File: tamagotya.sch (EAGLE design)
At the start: 62 parts, among them U100 ESP32-D2WD, U1000 TP4056, U1500 FS312F-G, U1550 FS8205, U200 UT-0206-P05FOLDED, U2000 MT3608, U2100 M3406, U300 4MB Flash, Y100 40Mhz 3.2X2.5

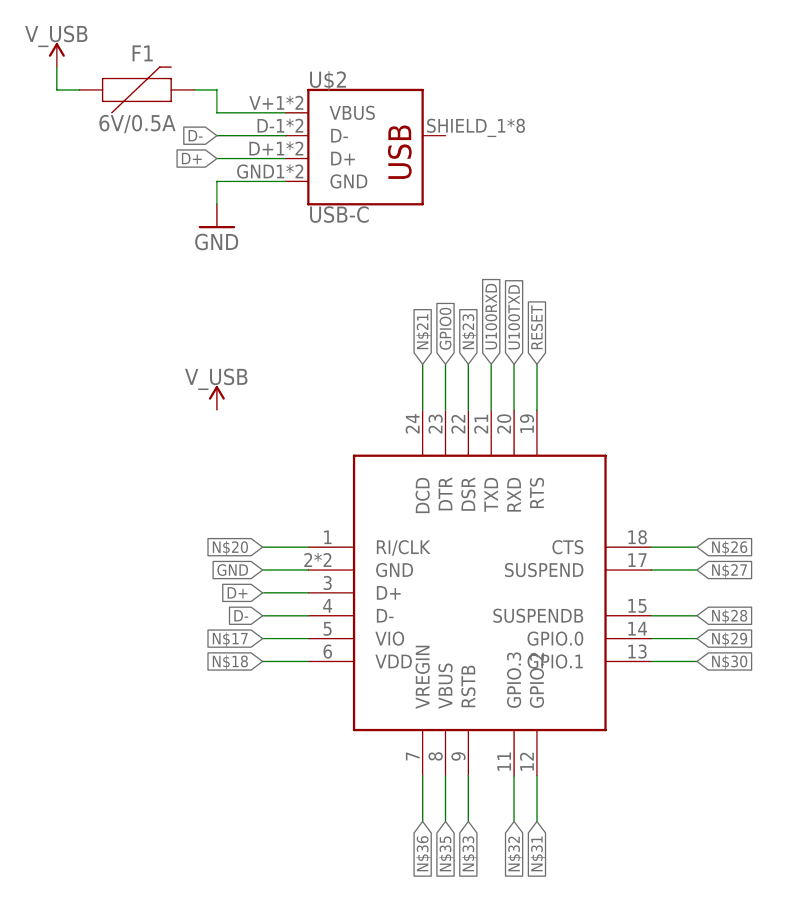
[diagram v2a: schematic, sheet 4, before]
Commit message: CP2102 now has adequate power circuitry, I believe
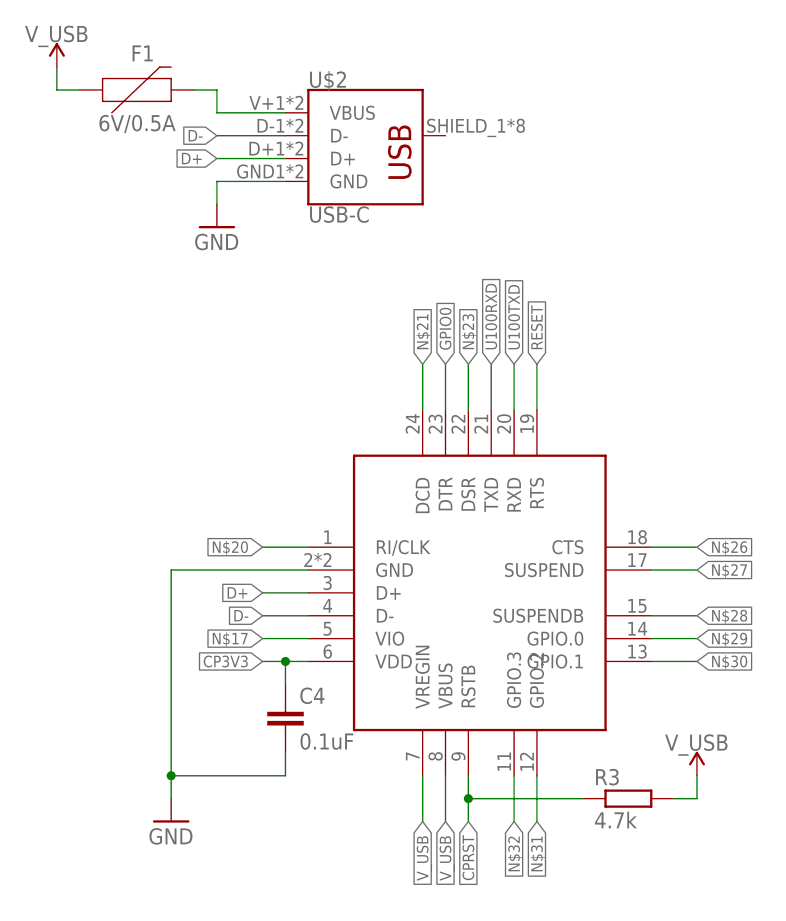
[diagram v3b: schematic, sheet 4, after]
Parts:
- added C4: 0.1uF, rcl:C-EUC0603
- added R3: 4.7k, rcl:R-EU_R0603
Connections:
- removed net N$18: U$3.VDD
- removed net N$33: U$3.RSTB
- removed net N$35: U$3.VBUS
- removed net N$36: U$3.VREGIN
- new net CP3V3: C4.1, U$3.VDD
- new net CPRST: R3.1, U$3.RSTB
- net GND: now also C4.2
- net V_USB: now also R3.2, U$3.VBUS, U$3.VREGIN
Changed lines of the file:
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@@
 <part name="GND27" library="SparkFun-PowerSymbols" library_urn="urn:adsk.eagle:library:530" deviceset="GND" device=""/>
 <part name="SUPPLY18" library="SparkFun-PowerSymbols" library_urn="urn:adsk.eagle:library:530" deviceset="3.3V" device=""/>
+<part name="C4" library="rcl" library_urn="urn:adsk.eagle:library:334" deviceset="C-EU" device="C0603" package3d_urn="urn:adsk.eagle:package:23616/2" value="0.1uF"/>
+<part name="GND28" library="supply1" library_urn="urn:adsk.eagle:library:371" deviceset="GND" device=""/>
+<part name="R3" library="rcl" library_urn="urn:adsk.eagle:library:334" deviceset="R-EU_" device="R0603" package3d_urn="urn:adsk.eagle:package:23555/2" value="4.7k"/>
 </parts>
 <sheets>
@@
 <attribute name="VALUE" x="15.24" y="119.634" size="1.778" layer="96" align="bottom-center"/>
 </instance>
-<instance part="SUPPLY17" gate="G$1" x="33.02" y="78.74" smashed="yes">
-<attribute name="VALUE" x="33.02" y="81.534" size="1.778" layer="96" align="bottom-center"/>
+<instance part="SUPPLY17" gate="G$1" x="86.36" y="38.1" smashed="yes">
+<attribute name="VALUE" x="86.36" y="40.894" size="1.778" layer="96" align="bottom-center"/>
+</instance>
+<instance part="C4" gate="G$1" x="40.64" y="45.72" smashed="yes">
+<attribute name="NAME" x="42.164" y="46.101" size="1.778" layer="95"/>
+<attribute name="VALUE" x="42.164" y="41.021" size="1.778" layer="96"/>
+</instance>
+<instance part="GND28" gate="1" x="27.94" y="33.02" smashed="yes">
+<attribute name="VALUE" x="25.4" y="30.48" size="1.778" layer="96"/>
+</instance>
+<instance part="R3" gate="G$1" x="78.74" y="35.56" smashed="yes">
+<attribute name="NAME" x="74.93" y="37.0586" size="1.778" layer="95"/>
+<attribute name="VALUE" x="74.93" y="32.258" size="1.778" layer="96"/>
 </instance>
 </instances>
@@
 </segment>
 <segment>
+<pinref part="C4" gate="G$1" pin="2"/>
+<wire x1="40.64" y1="40.64" x2="40.64" y2="38.1" width="0.1524" layer="91"/>
+<wire x1="40.64" y1="38.1" x2="27.94" y2="38.1" width="0.1524" layer="91"/>
+<pinref part="GND28" gate="1" pin="GND"/>
+<wire x1="27.94" y1="38.1" x2="27.94" y2="35.56" width="0.1524" layer="91"/>
 <pinref part="U$3" gate="G$1" pin="GND"/>
-<wire x1="43.18" y1="60.96" x2="38.1" y2="60.96" width="0.1524" layer="91"/>
-<label x="38.1" y="60.96" size="1.27" layer="95" rot="R180" xref="yes"/>
+<wire x1="43.18" y1="60.96" x2="27.94" y2="60.96" width="0.1524" layer="91"/>
+<wire x1="27.94" y1="60.96" x2="27.94" y2="38.1" width="0.1524" layer="91"/>
+<junction x="27.94" y="38.1"/>
 </segment>
 </net>
@@
 </segment>
 </net>
-<net name="N$18" class="0">
+<net name="CP3V3" class="0">
 <segment>
 <pinref part="U$3" gate="G$1" pin="VDD"/>
-<wire x1="43.18" y1="50.8" x2="38.1" y2="50.8" width="0.1524" layer="91"/>
+<wire x1="43.18" y1="50.8" x2="40.64" y2="50.8" width="0.1524" layer="91"/>
 <label x="38.1" y="50.8" size="1.27" layer="95" rot="R180" xref="yes"/>
+<pinref part="C4" gate="G$1" pin="1"/>
+<wire x1="40.64" y1="50.8" x2="38.1" y2="50.8" width="0.1524" layer="91"/>
+<wire x1="40.64" y1="48.26" x2="40.64" y2="50.8" width="0.1524" layer="91"/>
+<junction x="40.64" y="50.8"/>
 </segment>
 </net>
@@
 </segment>
 </net>
-<net name="N$33" class="0">
+<net name="CPRST" class="0">
 <segment>
 <pinref part="U$3" gate="G$1" pin="RSTB"/>
-<wire x1="60.96" y1="38.1" x2="60.96" y2="33.02" width="0.1524" layer="91"/>
+<wire x1="60.96" y1="38.1" x2="60.96" y2="35.56" width="0.1524" layer="91"/>
 <label x="60.96" y="33.02" size="1.27" layer="95" rot="R270" xref="yes"/>
-</segment>
-</net>
-<net name="N$35" class="0">
-<segment>
-<pinref part="U$3" gate="G$1" pin="VBUS"/>
-<wire x1="58.42" y1="38.1" x2="58.42" y2="33.02" width="0.1524" layer="91"/>
-<label x="58.42" y="33.02" size="1.27" layer="95" rot="R270" xref="yes"/>
-</segment>
-</net>
-<net name="N$36" class="0">
-<segment>
-<pinref part="U$3" gate="G$1" pin="VREGIN"/>
-<wire x1="55.88" y1="38.1" x2="55.88" y2="33.02" width="0.1524" layer="91"/>
-<label x="55.88" y="33.02" size="1.27" layer="95" rot="R270" xref="yes"/>
+<pinref part="R3" gate="G$1" pin="1"/>
+<wire x1="60.96" y1="35.56" x2="60.96" y2="33.02" width="0.1524" layer="91"/>
+<wire x1="73.66" y1="35.56" x2="60.96" y2="35.56" width="0.1524" layer="91"/>
+<junction x="60.96" y="35.56"/>
 </segment>
 </net>
@@
 <pinref part="SUPPLY13" gate="G$1" pin="V_USB"/>
 </segment>
-</net>
+<segment>
+<pinref part="U$3" gate="G$1" pin="VBUS"/>
+<wire x1="58.42" y1="38.1" x2="58.42" y2="33.02" width="0.1524" layer="91"/>
+<label x="58.42" y="33.02" size="1.27" layer="95" rot="R270" xref="yes"/>
+</segment>
+<segment>
+<pinref part="U$3" gate="G$1" pin="VREGIN"/>
+<wire x1="55.88" y1="38.1" x2="55.88" y2="33.02" width="0.1524" layer="91"/>
+<label x="55.88" y="33.02" size="1.27" layer="95" rot="R270" xref="yes"/>
+</segment>
+<segment>
+<pinref part="R3" gate="G$1" pin="2"/>
+<wire x1="83.82" y1="35.56" x2="86.36" y2="35.56" width="0.1524" layer="91"/>
+<pinref part="SUPPLY17" gate="G$1" pin="V_USB"/>
+<wire x1="86.36" y1="35.56" x2="86.36" y2="38.1" width="0.1524" layer="91"/>
+</segment>
+</net>

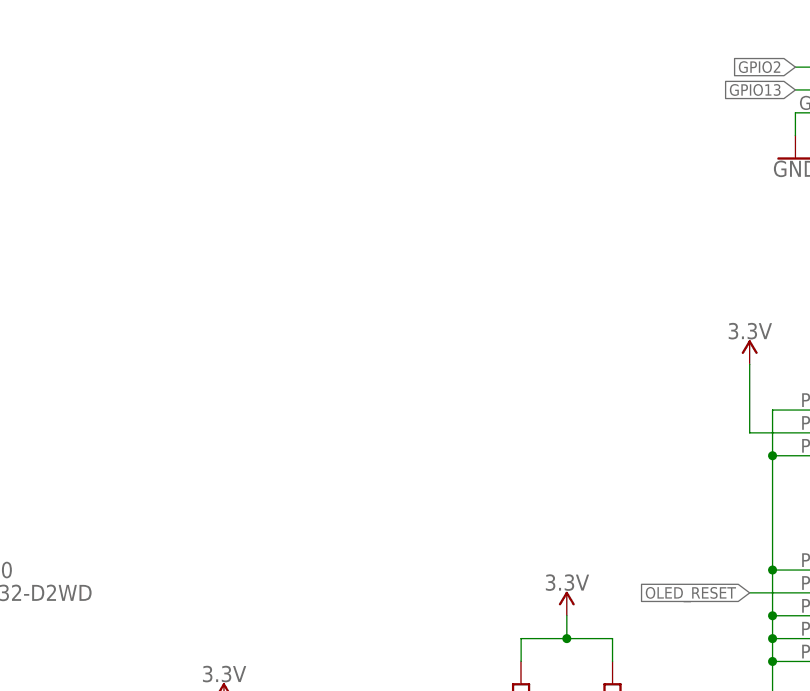
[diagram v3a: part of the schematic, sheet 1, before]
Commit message: Accellerometer ADXL345 with i2c + 1 interrupt.
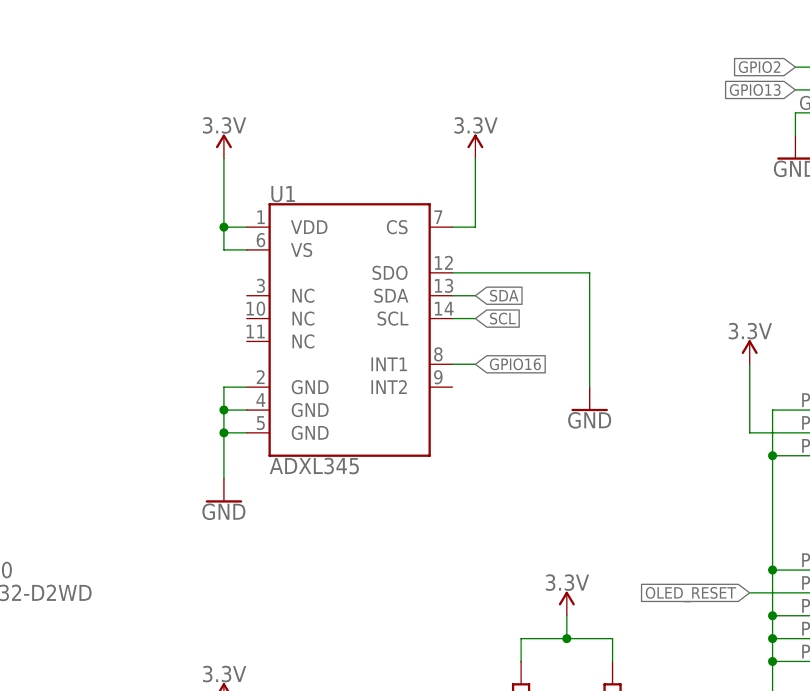
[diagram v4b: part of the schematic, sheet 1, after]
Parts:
- added U1: ADXL345, SparkFun-Sensors:ADXL345
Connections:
- net 3.3V: now also U1.CS, U1.VDD, U1.VS
- net GND: now also U1.GND@2, U1.GND@4, U1.GND@5, U1.SDO
- net GPIO16: now also U1.INT1
- net SCL: now also U1.SCL
- net SDA: now also U1.SDA
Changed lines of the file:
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@@
 <part name="GND28" library="supply1" library_urn="urn:adsk.eagle:library:371" deviceset="GND" device=""/>
 <part name="R3" library="rcl" library_urn="urn:adsk.eagle:library:334" deviceset="R-EU_" device="R0603" package3d_urn="urn:adsk.eagle:package:23555/2" value="4.7k"/>
+<part name="U1" library="SparkFun-Sensors" deviceset="ADXL345" device=""/>
+<part name="GND29" library="SparkFun-PowerSymbols" library_urn="urn:adsk.eagle:library:530" deviceset="GND" device=""/>
+<part name="GND30" library="SparkFun-PowerSymbols" library_urn="urn:adsk.eagle:library:530" deviceset="GND" device=""/>
+<part name="SUPPLY19" library="SparkFun-PowerSymbols" library_urn="urn:adsk.eagle:library:530" deviceset="3.3V" device=""/>
+<part name="SUPPLY20" library="SparkFun-PowerSymbols" library_urn="urn:adsk.eagle:library:530" deviceset="3.3V" device=""/>
 </parts>
 <sheets>
@@
 <attribute name="NAME" x="8.6614" y="92.71" size="1.778" layer="95" rot="R90"/>
 <attribute name="VALUE" x="13.462" y="92.71" size="1.778" layer="96" rot="R90"/>
+</instance>
+<instance part="U1" gate="G$1" x="132.08" y="134.62" smashed="yes">
+<attribute name="NAME" x="124.46" y="147.574" size="1.778" layer="95" font="vector"/>
+<attribute name="VALUE" x="124.46" y="119.126" size="1.778" layer="96" font="vector" align="top-left"/>
+</instance>
+<instance part="GND29" gate="1" x="160.02" y="124.46" smashed="yes">
+<attribute name="VALUE" x="160.02" y="124.206" size="1.778" layer="96" align="top-center"/>
+</instance>
+<instance part="GND30" gate="1" x="119.38" y="114.3" smashed="yes">
+<attribute name="VALUE" x="119.38" y="114.046" size="1.778" layer="96" align="top-center"/>
+</instance>
+<instance part="SUPPLY19" gate="G$1" x="119.38" y="152.4" smashed="yes">
+<attribute name="VALUE" x="119.38" y="155.194" size="1.778" layer="96" align="bottom-center"/>
+</instance>
+<instance part="SUPPLY20" gate="G$1" x="147.32" y="152.4" smashed="yes">
+<attribute name="VALUE" x="147.32" y="155.194" size="1.778" layer="96" align="bottom-center"/>
 </instance>
 </instances>
@@
 <wire x1="182.88" y1="154.94" x2="182.88" y2="157.48" width="0.1524" layer="91"/>
 </segment>
+<segment>
+<pinref part="U1" gate="G$1" pin="SDO"/>
+<wire x1="144.78" y1="139.7" x2="160.02" y2="139.7" width="0.1524" layer="91"/>
+<wire x1="160.02" y1="139.7" x2="160.02" y2="127" width="0.1524" layer="91"/>
+<pinref part="GND29" gate="1" pin="GND"/>
+</segment>
+<segment>
+<pinref part="U1" gate="G$1" pin="GND@2"/>
+<wire x1="121.92" y1="127" x2="119.38" y2="127" width="0.1524" layer="91"/>
+<wire x1="119.38" y1="127" x2="119.38" y2="124.46" width="0.1524" layer="91"/>
+<pinref part="U1" gate="G$1" pin="GND@4"/>
+<wire x1="119.38" y1="124.46" x2="121.92" y2="124.46" width="0.1524" layer="91"/>
+<wire x1="119.38" y1="124.46" x2="119.38" y2="121.92" width="0.1524" layer="91"/>
+<junction x="119.38" y="124.46"/>
+<pinref part="U1" gate="G$1" pin="GND@5"/>
+<wire x1="119.38" y1="121.92" x2="119.38" y2="116.84" width="0.1524" layer="91"/>
+<wire x1="121.92" y1="121.92" x2="119.38" y2="121.92" width="0.1524" layer="91"/>
+<junction x="119.38" y="121.92"/>
+<pinref part="GND30" gate="1" pin="GND"/>
+</segment>
 </net>
 <net name="GPIO16" class="0">
@@
 <wire x1="93.98" y1="55.88" x2="96.52" y2="55.88" width="0.1524" layer="91"/>
 <label x="96.52" y="55.88" size="1.27" layer="95" xref="yes"/>
+</segment>
+<segment>
+<pinref part="U1" gate="G$1" pin="INT1"/>
+<wire x1="144.78" y1="129.54" x2="147.32" y2="129.54" width="0.1524" layer="91"/>
+<label x="147.32" y="129.54" size="1.27" layer="95" xref="yes"/>
 </segment>
 </net>
@@
 <wire x1="254" y1="81.28" x2="254" y2="78.74" width="0.1524" layer="91"/>
 </segment>
+<segment>
+<pinref part="U1" gate="G$1" pin="VDD"/>
+<wire x1="121.92" y1="144.78" x2="119.38" y2="144.78" width="0.1524" layer="91"/>
+<wire x1="119.38" y1="144.78" x2="119.38" y2="152.4" width="0.1524" layer="91"/>
+<pinref part="SUPPLY19" gate="G$1" pin="3.3V"/>
+<pinref part="U1" gate="G$1" pin="VS"/>
+<wire x1="121.92" y1="142.24" x2="119.38" y2="142.24" width="0.1524" layer="91"/>
+<wire x1="119.38" y1="142.24" x2="119.38" y2="144.78" width="0.1524" layer="91"/>
+<junction x="119.38" y="144.78"/>
+</segment>
+<segment>
+<pinref part="U1" gate="G$1" pin="CS"/>
+<wire x1="144.78" y1="144.78" x2="147.32" y2="144.78" width="0.1524" layer="91"/>
+<wire x1="147.32" y1="144.78" x2="147.32" y2="152.4" width="0.1524" layer="91"/>
+<pinref part="SUPPLY20" gate="G$1" pin="3.3V"/>
+</segment>
 </net>
 <net name="GPIO14" class="0">
@@
 <label x="60.96" y="30.48" size="1.27" layer="95" rot="R270" xref="yes"/>
 </segment>
+<segment>
+<pinref part="U1" gate="G$1" pin="SCL"/>
+<wire x1="144.78" y1="134.62" x2="147.32" y2="134.62" width="0.1524" layer="91"/>
+<label x="147.32" y="134.62" size="1.27" layer="95" xref="yes"/>
+</segment>
 </net>
 <net name="SDA" class="0">
@@
 <label x="58.42" y="30.48" size="1.27" layer="95" rot="R270" xref="yes"/>
 </segment>
-</net>
+<segment>
+<pinref part="U1" gate="G$1" pin="SDA"/>
+<wire x1="144.78" y1="137.16" x2="147.32" y2="137.16" width="0.1524" layer="91"/>
+<label x="147.32" y="137.16" size="1.27" layer="95" xref="yes"/>
+</segment>
+</net>

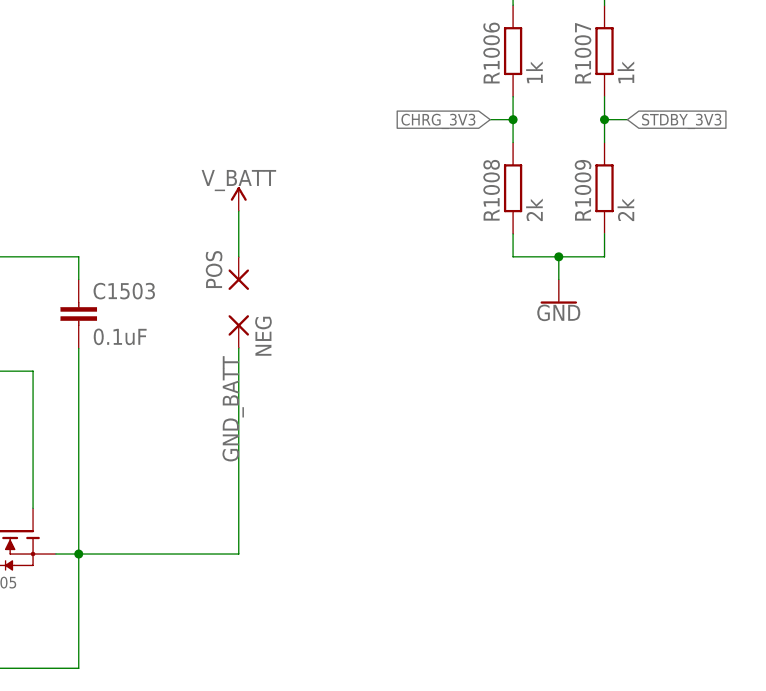
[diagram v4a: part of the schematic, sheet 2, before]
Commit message: Done: ADC sensing battery voltage.
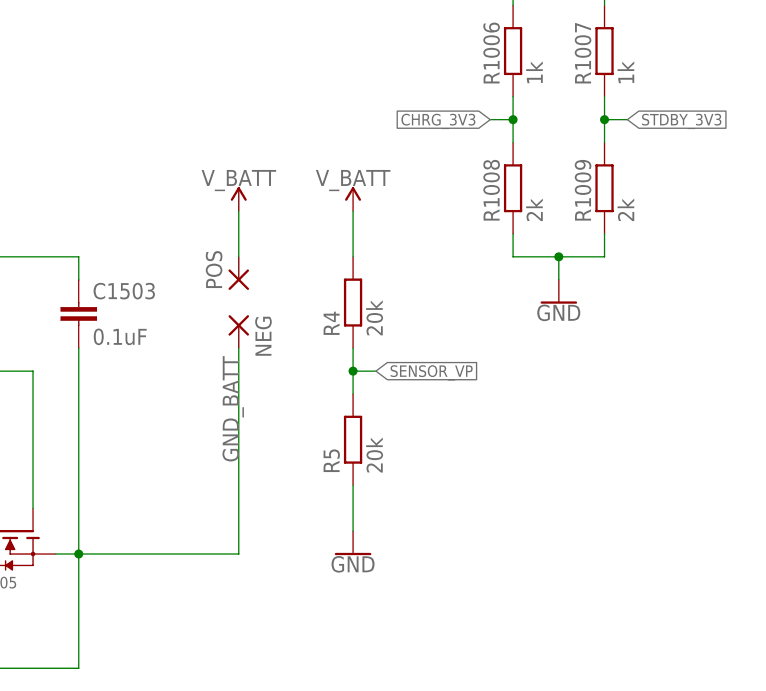
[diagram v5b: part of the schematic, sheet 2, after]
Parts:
- added R4, R5: 20k, rcl:R-EU_R0603
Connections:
- net GND: now also R5.1
- net SENSOR_VP: now also R4.1, R5.2
- net V_BATT: now also R4.2
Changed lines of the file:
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@@
 <part name="SUPPLY19" library="SparkFun-PowerSymbols" library_urn="urn:adsk.eagle:library:530" deviceset="3.3V" device=""/>
 <part name="SUPPLY20" library="SparkFun-PowerSymbols" library_urn="urn:adsk.eagle:library:530" deviceset="3.3V" device=""/>
+<part name="R4" library="rcl" library_urn="urn:adsk.eagle:library:334" deviceset="R-EU_" device="R0603" package3d_urn="urn:adsk.eagle:package:23555/2" value="20k"/>
+<part name="R5" library="rcl" library_urn="urn:adsk.eagle:library:334" deviceset="R-EU_" device="R0603" package3d_urn="urn:adsk.eagle:package:23555/2" value="20k"/>
+<part name="SUPPLY22" library="SparkFun-PowerSymbols" library_urn="urn:adsk.eagle:library:530" deviceset="V_BATT" device=""/>
+<part name="GND31" library="SparkFun-PowerSymbols" library_urn="urn:adsk.eagle:library:530" deviceset="GND" device=""/>
 </parts>
 <sheets>
@@
 <attribute name="VALUE" x="125.222" y="72.517" size="1.778" layer="96" rot="R90"/>
 </instance>
+<instance part="R4" gate="G$1" x="134.62" y="71.12" smashed="yes" rot="R90">
+<attribute name="NAME" x="133.1214" y="67.31" size="1.778" layer="95" rot="R90"/>
+<attribute name="VALUE" x="137.922" y="67.31" size="1.778" layer="96" rot="R90"/>
+</instance>
+<instance part="R5" gate="G$1" x="134.62" y="55.88" smashed="yes" rot="R90">
+<attribute name="NAME" x="133.1214" y="52.07" size="1.778" layer="95" rot="R90"/>
+<attribute name="VALUE" x="137.922" y="52.07" size="1.778" layer="96" rot="R90"/>
+</instance>
+<instance part="SUPPLY22" gate="G$1" x="134.62" y="81.28" smashed="yes">
+<attribute name="VALUE" x="134.62" y="84.074" size="1.778" layer="96" align="bottom-center"/>
+</instance>
+<instance part="GND31" gate="1" x="134.62" y="43.18" smashed="yes">
+<attribute name="VALUE" x="134.62" y="42.926" size="1.778" layer="96" align="top-center"/>
+</instance>
 </instances>
 <busses>
@@
 <pinref part="SUPPLY15" gate="G$1" pin="V_BATT"/>
 </segment>
+<segment>
+<pinref part="R4" gate="G$1" pin="2"/>
+<wire x1="134.62" y1="76.2" x2="134.62" y2="81.28" width="0.1524" layer="91"/>
+<pinref part="SUPPLY22" gate="G$1" pin="V_BATT"/>
+</segment>
 </net>
 <net name="N$4" class="0">
@@
 <junction x="157.48" y="76.2"/>
 <pinref part="GND20" gate="1" pin="GND"/>
+</segment>
+<segment>
+<pinref part="R5" gate="G$1" pin="1"/>
+<wire x1="134.62" y1="50.8" x2="134.62" y2="45.72" width="0.1524" layer="91"/>
+<pinref part="GND31" gate="1" pin="GND"/>
 </segment>
 </net>
@@
 </segment>
 </net>
+<net name="SENSOR_VP" class="0">
+<segment>
+<pinref part="R5" gate="G$1" pin="2"/>
+<pinref part="R4" gate="G$1" pin="1"/>
+<wire x1="134.62" y1="60.96" x2="134.62" y2="63.5" width="0.1524" layer="91"/>
+<wire x1="134.62" y1="63.5" x2="134.62" y2="66.04" width="0.1524" layer="91"/>
+<wire x1="134.62" y1="63.5" x2="137.16" y2="63.5" width="0.1524" layer="91"/>
+<junction x="134.62" y="63.5"/>
+<label x="137.16" y="63.5" size="1.27" layer="95" xref="yes"/>
+</segment>
+</net>
